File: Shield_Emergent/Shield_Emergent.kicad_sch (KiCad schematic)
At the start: 19 parts, among them J1 Conn_01x02_Female, J2 Conn_01x04_Male, J3 Conn_01x02_Female, J4 Conn_01x04_Male, U1 Raspberri_Pi_Pico, U2 TPS2553, U3 TPS2553

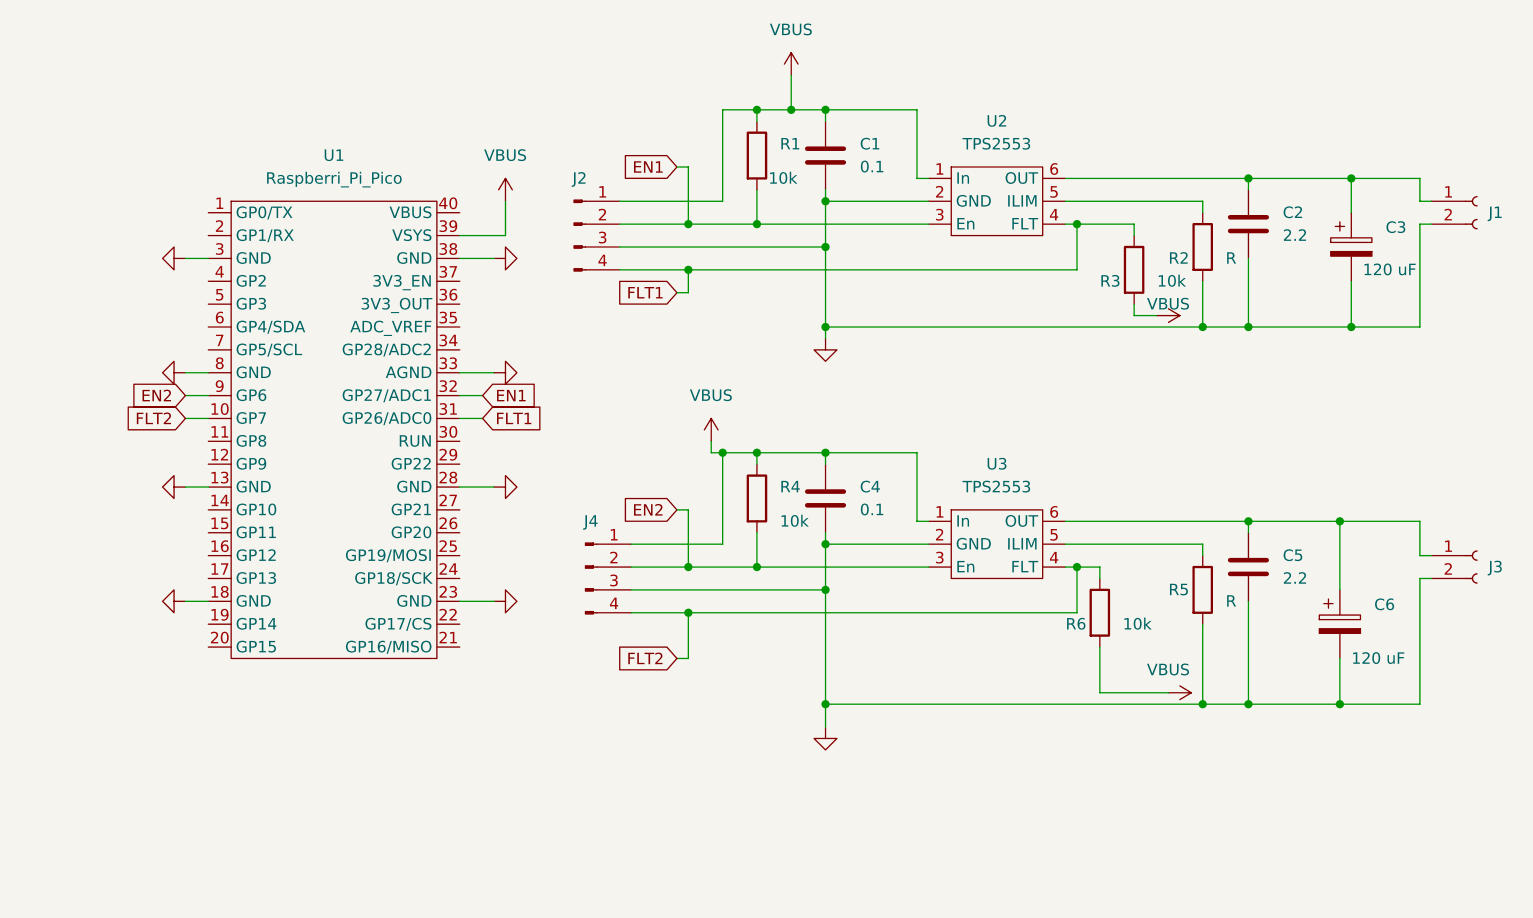
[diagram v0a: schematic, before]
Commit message: v1.1 Circuit was corrected, GND was enfrced
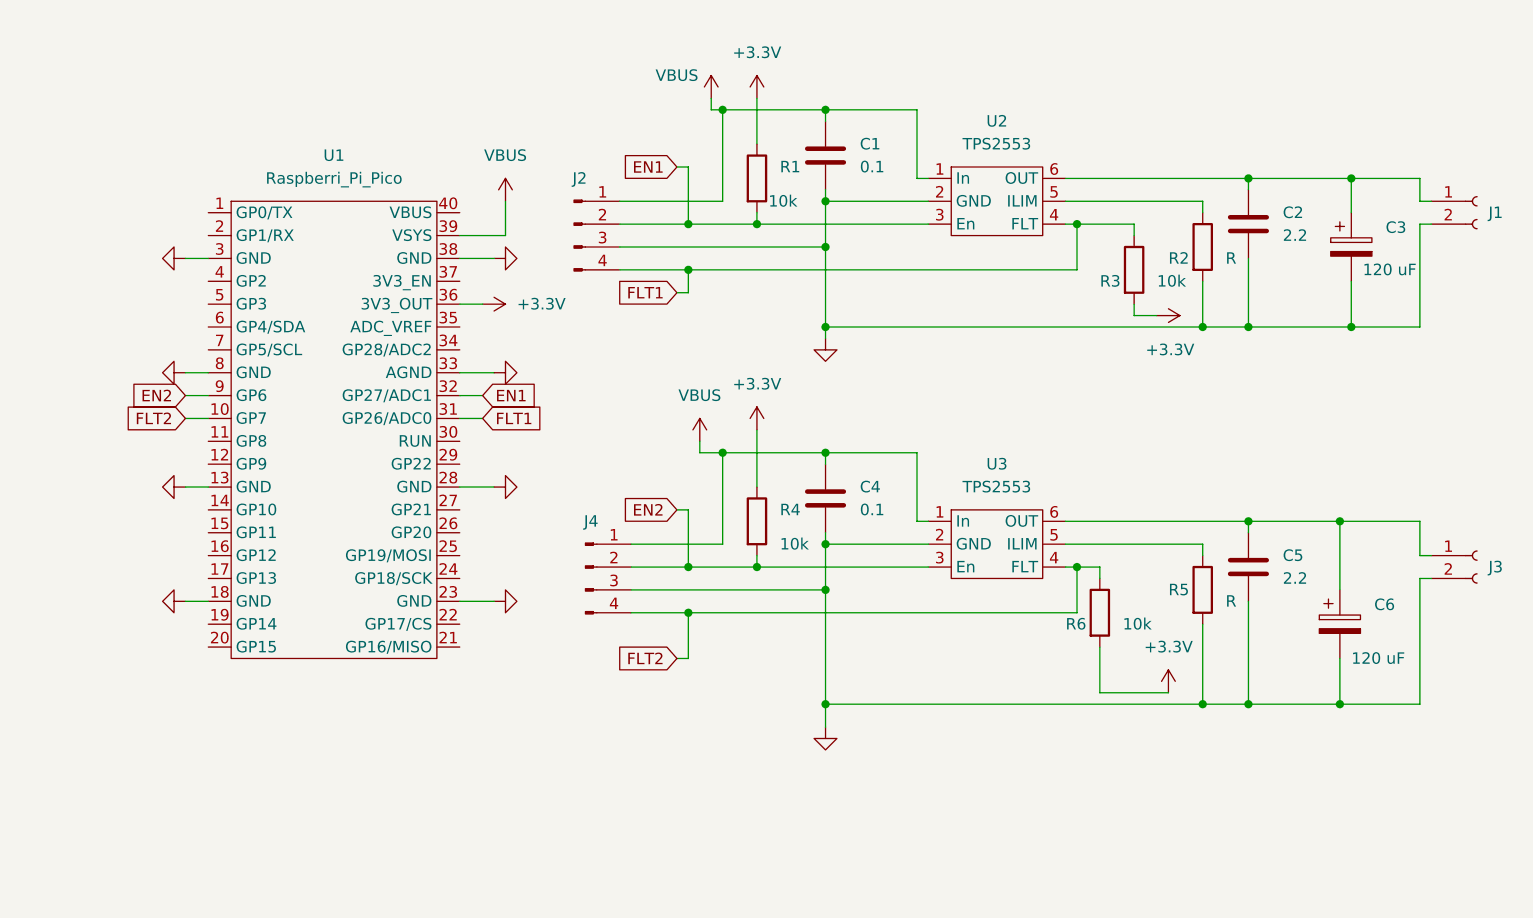
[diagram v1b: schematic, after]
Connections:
- net VBUS: no longer R1.1, R3.2, R4.1, R6.2
- net +3V3: now reaches U1.36 (3V3_OUT)
- net +3V3: now also R1.1, R3.2, R4.1, R6.2
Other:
- moved on the sheet: R1, R4

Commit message: v1.3 Power of RPI_PICO and Shield was splitted
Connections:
- net VBUS: no longer U1.39 (VSYS)
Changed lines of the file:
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@@
-    (stroke (width 0) (type default) (color 0 0 0 0))
-  )
-  (wire (pts (xy 78.74 34.29) (xy 78.74 38.1))
     (stroke (width 0) (type default) (color 0 0 0 0))
   )
@@
   )
   (wire (pts (xy 92.71 74.93) (xy 99.06 74.93))
-    (stroke (width 0) (type default) (color 0 0 0 0))
-  )
-  (wire (pts (xy 78.74 38.1) (xy 73.66 38.1))
     (stroke (width 0) (type default) (color 0 0 0 0))
   )
@@
     (pin "1")
     (pin "2")
-  )
-  (symbol (lib_id "power:VBUS") (at 78.74 34.29 0) (unit 1)
-    (in_bom yes) (on_board yes) (fields_autoplaced)
-    (property "Reference" "#PWR0106" (id 0) (at 78.74 38.1 0)
-      (effects (font (size 1.27 1.27)) hide)
-    )
-    (property "Value" "VBUS" (id 1) (at 78.74 29.21 0))
-    (property "Footprint" "" (id 2) (at 78.74 34.29 0)
-      (effects (font (size 1.27 1.27)) hide)
-    )
-    (property "Datasheet" "" (id 3) (at 78.74 34.29 0)
-      (effects (font (size 1.27 1.27)) hide)
-    )
-    (pin "1")
   )
   (symbol (lib_id "power:GND") (at 43.18 66.04 270) (unit 1)
@@
       (reference "#PWR0105") (unit 1) (value "+3.3V") (footprint "")
     )
-    (path "/3d3713bb-0af7-4c8c-b880-4e10bd4e1bde"
-      (reference "#PWR0106") (unit 1) (value "VBUS") (footprint "")
-    )
     (path "/b9423a98-fc7e-4a86-a1b8-2c19cb1900ad"

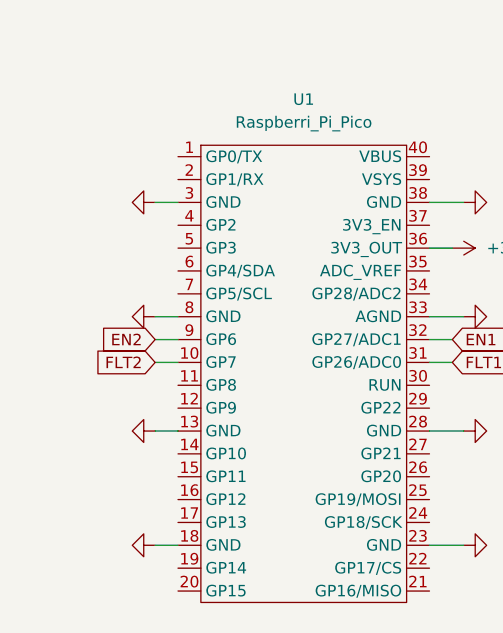
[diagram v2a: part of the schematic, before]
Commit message: v1.4 four Buttons protos were added
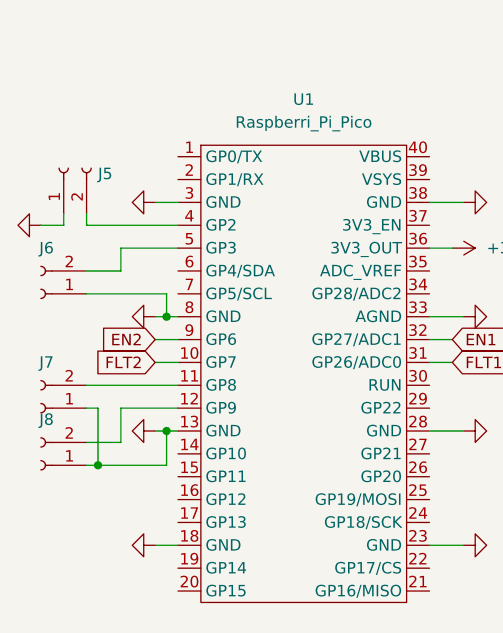
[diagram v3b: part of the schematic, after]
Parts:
- added J5, J6, J7, J8: Conn_01x02_Female, Connector_PinSocket_2.54mm:PinSocket_1x02_P2.54mm_Vertical, symbol Connector:Conn_01x02_Female
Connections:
- net GND: now also J5.1 (Pin_1), J6.1 (Pin_1), J7.1 (Pin_1), J8.1 (Pin_1)
- net at U1.11 (GP8): now also J7.2 (Pin_2)
- net at U1.12 (GP9): now also J8.2 (Pin_2)
- net at U1.4 (GP2): now also J5.2 (Pin_2)
- net at U1.5 (GP3): now also J6.2 (Pin_2)

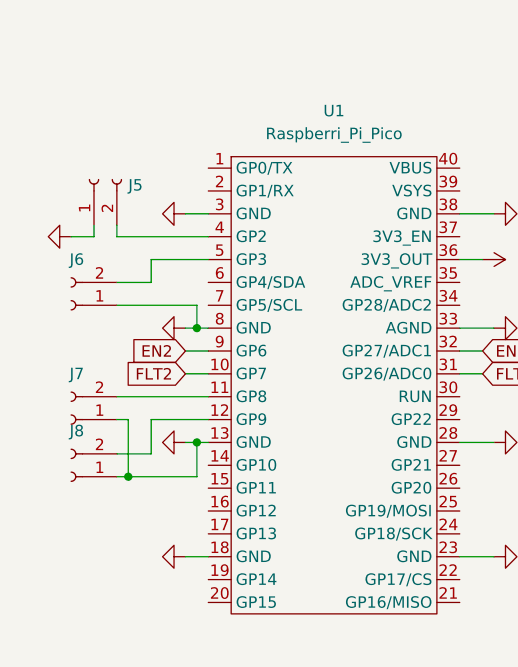
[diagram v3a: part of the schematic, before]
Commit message: v1.5 Buttons Polarity was changed
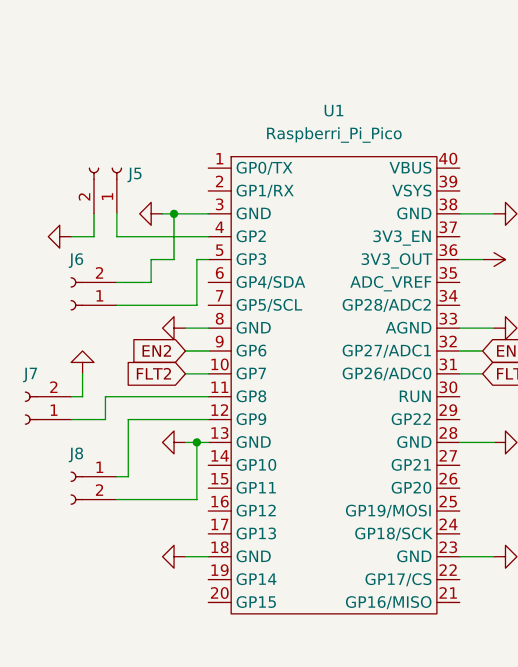
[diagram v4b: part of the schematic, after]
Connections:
- net GND: now also J5.2 (Pin_2), J6.2 (Pin_2), J7.2 (Pin_2), J8.2 (Pin_2); no longer J5.1 (Pin_1), J6.1 (Pin_1), J7.1 (Pin_1), J8.1 (Pin_1)
- net at U1.4 (GP2): now also J5.1 (Pin_1); no longer J5.2 (Pin_2)
- net at U1.11 (GP8): now also J7.1 (Pin_1); no longer J7.2 (Pin_2)
- net at U1.12 (GP9): now also J8.1 (Pin_1); no longer J8.2 (Pin_2)
- net at U1.5 (GP3): now also J6.1 (Pin_1); no longer J6.2 (Pin_2)
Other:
- moved on the sheet: J5, J7, J8

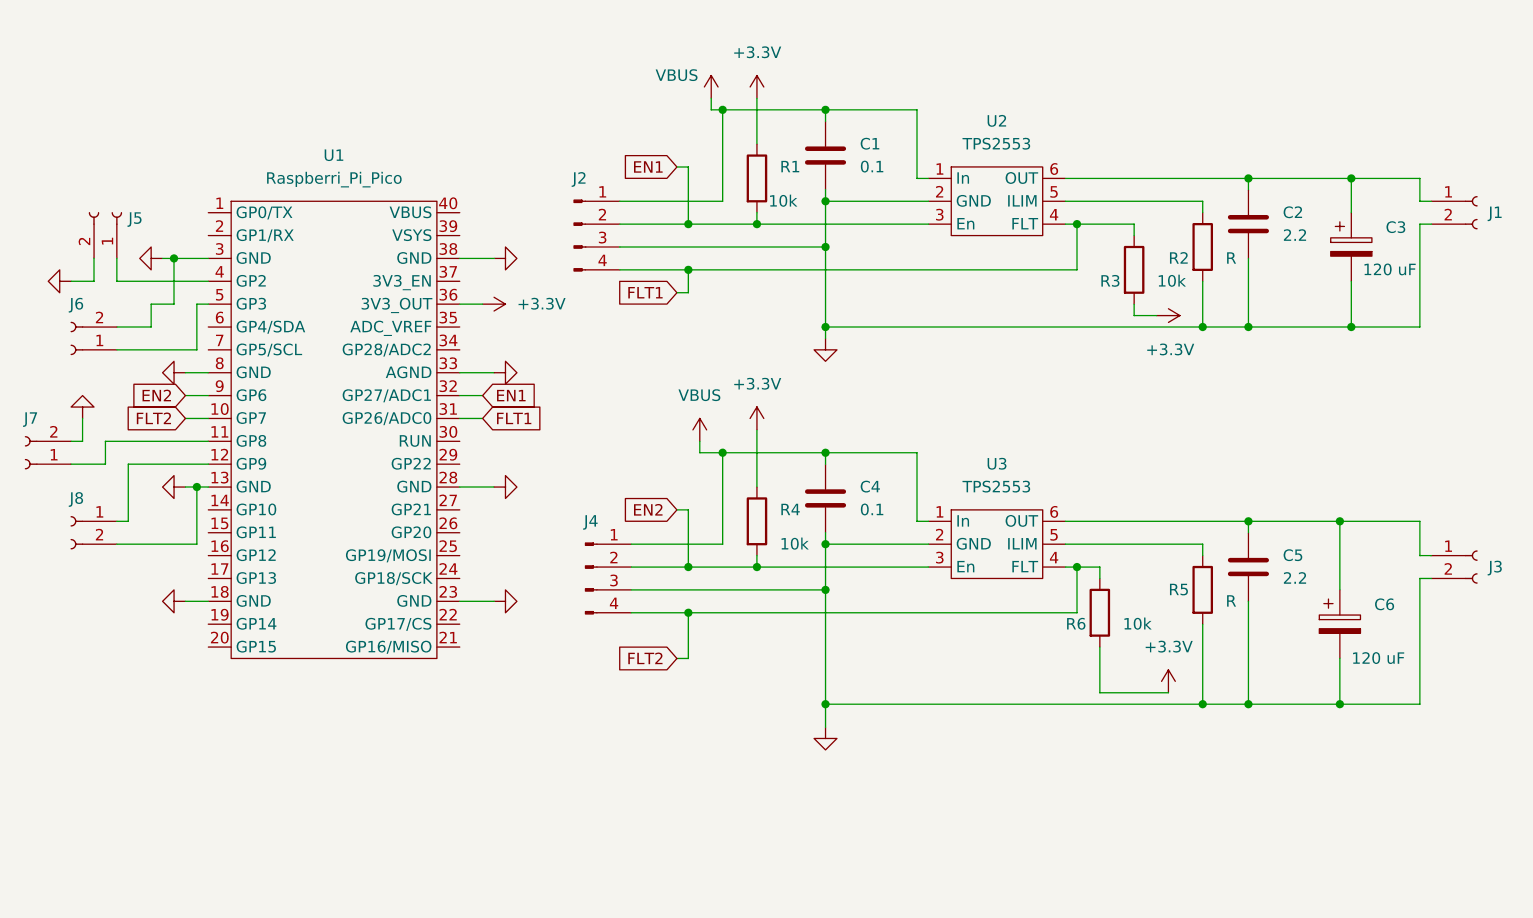
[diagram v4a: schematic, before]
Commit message: v1.6 single connector for all purposes was added
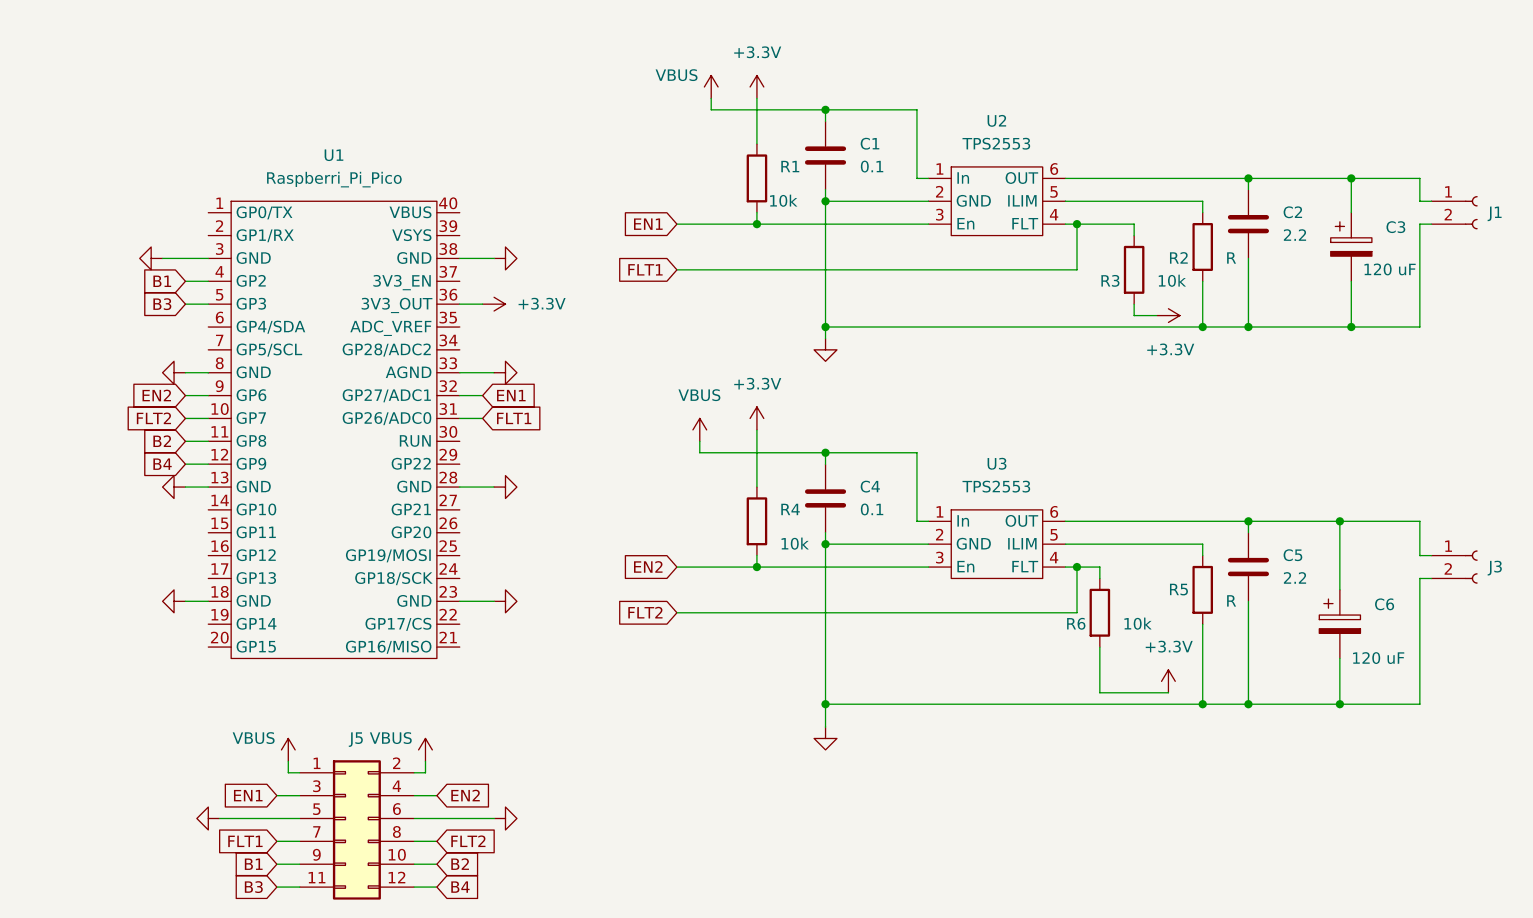
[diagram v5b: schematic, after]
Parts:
- removed J2, J4: Conn_01x04_Male, Connector_PinSocket_2.54mm:PinSocket_1x04_P2.54mm_Vertical, symbol Connector:Conn_01x04_Male
- removed J5, J6, J7, J8: Conn_01x02_Female, Connector_PinSocket_2.54mm:PinSocket_1x02_P2.54mm_Vertical, symbol Connector:Conn_01x02_Female
- added J5: Conn_02x06_Odd_Even, Connector_PinHeader_2.54mm:PinHeader_2x06_P2.54mm_Vertical, symbol Connector_Generic:Conn_02x06_Odd_Even
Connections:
- net EN1: now also J5.3 (Pin_3)
- net EN2: now also J5.4 (Pin_4)
- net FLT1: now also J5.7 (Pin_7)
- net FLT2: now also J5.8 (Pin_8)
- net GND: now also J5.5 (Pin_5), J5.6 (Pin_6)
- net VBUS: now also J5.1 (Pin_1), J5.2 (Pin_2)
- net B1: now reaches U1.4 (GP2)
- net B1: now also J5.9 (Pin_9)
- net B2: now reaches U1.11 (GP8)
- net B2: now also J5.10 (Pin_10)
- net B4: now reaches U1.12 (GP9)
- net B4: now also J5.12 (Pin_12)
- net B3: now reaches U1.5 (GP3)
- net B3: now also J5.11 (Pin_11)

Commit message: v1.7 DRC was conducted
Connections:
- net B1: now also J5.12 (Pin_12); no longer J5.9 (Pin_9)
- net B2: now also J5.11 (Pin_11); no longer J5.10 (Pin_10)
- net B3: now also J5.10 (Pin_10); no longer J5.11 (Pin_11)
- net B4: now also J5.9 (Pin_9); no longer J5.12 (Pin_12)
